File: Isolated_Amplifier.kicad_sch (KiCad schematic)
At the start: 12 parts, among them U3 AMC3311QDWERQ1

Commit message: isolated precharge from fuse
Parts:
- added C15: 1n, Capacitor_SMD:C_0603_1608Metric_Pad1.08x0.95mm_HandSolder, symbol Device:C
- renumbered C15 to C16, C16 to C17, C17 to C18, C18 to C19
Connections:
- net DCDC_OUT: now also C15.1
- net HVGND: now also C15.2
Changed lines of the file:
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@@
+	(wire
+		(pts
+			(xy 39.37 74.93) (xy 39.37 77.47)
+		)
+		(stroke
+			(width 0)
+			(type default)
+		)
+	)
 	(wire
 		(pts
@@
 	(wire
 		(pts
+			(xy 39.37 85.09) (xy 39.37 88.9)
+		)
+		(stroke
+			(width 0)
+			(type default)
+		)
+	)
+	(wire
+		(pts
 			(xy 137.16 45.72) (xy 137.16 50.8)
 		)
@@
 		)
 	)
-	(label "ISO_AMP"
+	(label "DCDC_HGND"
 		(at 16.51 25.4 0)
 		(effects
@@
 		)
 	)
-	(label "ISO_AMP"
+	(label "DCDC_HGND"
 		(at 16.51 45.72 0)
 		(effects
@@
 		)
 	)
+	(label "DCDC_OUT"
+		(at 39.37 74.93 180)
+		(effects
+			(font
+				(size 1.27 1.27)
+			)
+			(justify right bottom)
+		)
+	)
 	(label "HLDO_IN"
 		(at 46.99 35.56 180)
@@
 		)
 	)
-	(label "ISO_AMP"
+	(label "DCDC_HGND"
 		(at 52.07 31.75 0)
 		(effects
@@
 			)
 			(justify left)
+		)
+	)
+	(hierarchical_label "HVGND"
+		(shape bidirectional)
+		(at 39.37 88.9 180)
+		(effects
+			(font
+				(size 1.27 1.27)
+			)
+			(justify right)
 		)
 	)
@@
 			(project "PS-PrechargeBoard"
 				(path "/74d17fe6-68d4-4bd7-954a-e2bbb58b1f1e/6627985a-aef4-4302-9d05-a969136ea8f4/03979947-561d-482f-9fca-eedcd558d33d"
-					(reference "C20")
+					(reference "C21")
 					(unit 1)
 				)
@@
 				)
 				(path "/74d17fe6-68d4-4bd7-954a-e2bbb58b1f1e/c9d052f0-39c4-441f-8d4e-0430a3425be4/03979947-561d-482f-9fca-eedcd558d33d"
-					(reference "C65")
+					(reference "C68")
 					(unit 1)
 				)
 				(path "/74d17fe6-68d4-4bd7-954a-e2bbb58b1f1e/c9d052f0-39c4-441f-8d4e-0430a3425be4/4cf09e58-0892-4fb3-a566-fe1392b5d663"
-					(reference "C57")
+					(reference "C59")
 					(unit 1)
 				)
@@
 		(in_pos_files yes)
 		(dnp no)
-		(property "Reference" "C18"
+		(property "Reference" "C19"
 			(at 167.894 37.084 90)
 			(show_name no)
@@
 			(project "PS-PrechargeBoard"
 				(path "/74d17fe6-68d4-4bd7-954a-e2bbb58b1f1e/6627985a-aef4-4302-9d05-a969136ea8f4/03979947-561d-482f-9fca-eedcd558d33d"
-					(reference "C26")
+					(reference "C28")
 					(unit 1)
 				)
 				(path "/74d17fe6-68d4-4bd7-954a-e2bbb58b1f1e/6627985a-aef4-4302-9d05-a969136ea8f4/4cf09e58-0892-4fb3-a566-fe1392b5d663"
-					(reference "C18")
+					(reference "C19")
 					(unit 1)
 				)
 				(path "/74d17fe6-68d4-4bd7-954a-e2bbb58b1f1e/c9d052f0-39c4-441f-8d4e-0430a3425be4/03979947-561d-482f-9fca-eedcd558d33d"
-					(reference "C71")
+					(reference "C75")
 					(unit 1)
 				)
 				(path "/74d17fe6-68d4-4bd7-954a-e2bbb58b1f1e/c9d052f0-39c4-441f-8d4e-0430a3425be4/4cf09e58-0892-4fb3-a566-fe1392b5d663"
-					(reference "C63")
+					(reference "C66")
 					(unit 1)
 				)
@@
 			(project "PS-PrechargeBoard"
 				(path "/74d17fe6-68d4-4bd7-954a-e2bbb58b1f1e/6627985a-aef4-4302-9d05-a969136ea8f4/03979947-561d-482f-9fca-eedcd558d33d"
-					(reference "C19")
+					(reference "C20")
 					(unit 1)
 				)
@@
 				)
 				(path "/74d17fe6-68d4-4bd7-954a-e2bbb58b1f1e/c9d052f0-39c4-441f-8d4e-0430a3425be4/03979947-561d-482f-9fca-eedcd558d33d"
-					(reference "C64")
+					(reference "C67")
 					(unit 1)
 				)
 				(path "/74d17fe6-68d4-4bd7-954a-e2bbb58b1f1e/c9d052f0-39c4-441f-8d4e-0430a3425be4/4cf09e58-0892-4fb3-a566-fe1392b5d663"
-					(reference "C56")
+					(reference "C58")
 					(unit 1)
 				)
@@
 			(project "PS-PrechargeBoard"
 				(path "/74d17fe6-68d4-4bd7-954a-e2bbb58b1f1e/6627985a-aef4-4302-9d05-a969136ea8f4/03979947-561d-482f-9fca-eedcd558d33d"
-					(reference "C22")
+					(reference "C23")
 					(unit 1)
 				)
@@
 				)
 				(path "/74d17fe6-68d4-4bd7-954a-e2bbb58b1f1e/c9d052f0-39c4-441f-8d4e-0430a3425be4/03979947-561d-482f-9fca-eedcd558d33d"
-					(reference "C67")
+					(reference "C70")
 					(unit 1)
 				)
 				(path "/74d17fe6-68d4-4bd7-954a-e2bbb58b1f1e/c9d052f0-39c4-441f-8d4e-0430a3425be4/4cf09e58-0892-4fb3-a566-fe1392b5d663"
-					(reference "C59")
+					(reference "C61")
 					(unit 1)
 				)
@@
 		(in_pos_files yes)
 		(dnp no)
-		(property "Reference" "C15"
+		(property "Reference" "C16"
 			(at 142.24 21.844 90)
 			(show_name no)
@@
 			(project "PS-PrechargeBoard"
 				(path "/74d17fe6-68d4-4bd7-954a-e2bbb58b1f1e/6627985a-aef4-4302-9d05-a969136ea8f4/03979947-561d-482f-9fca-eedcd558d33d"
-					(reference "C23")
+					(reference "C25")
 					(unit 1)
 				)
 				(path "/74d17fe6-68d4-4bd7-954a-e2bbb58b1f1e/6627985a-aef4-4302-9d05-a969136ea8f4/4cf09e58-0892-4fb3-a566-fe1392b5d663"
-					(reference "C15")
+					(reference "C16")
 					(unit 1)
 				)
 				(path "/74d17fe6-68d4-4bd7-954a-e2bbb58b1f1e/c9d052f0-39c4-441f-8d4e-0430a3425be4/03979947-561d-482f-9fca-eedcd558d33d"
-					(reference "C68")
+					(reference "C72")
 					(unit 1)
 				)
 				(path "/74d17fe6-68d4-4bd7-954a-e2bbb58b1f1e/c9d052f0-39c4-441f-8d4e-0430a3425be4/4cf09e58-0892-4fb3-a566-fe1392b5d663"
-					(reference "C60")
+					(reference "C63")
 					(unit 1)
 				)
@@
 			(project "PS-PrechargeBoard"
 				(path "/74d17fe6-68d4-4bd7-954a-e2bbb58b1f1e/6627985a-aef4-4302-9d05-a969136ea8f4/03979947-561d-482f-9fca-eedcd558d33d"
-					(reference "C21")
+					(reference "C22")
 					(unit 1)
 				)
@@
 				)
 				(path "/74d17fe6-68d4-4bd7-954a-e2bbb58b1f1e/c9d052f0-39c4-441f-8d4e-0430a3425be4/03979947-561d-482f-9fca-eedcd558d33d"
-					(reference "C66")
+					(reference "C69")
 					(unit 1)
 				)
 				(path "/74d17fe6-68d4-4bd7-954a-e2bbb58b1f1e/c9d052f0-39c4-441f-8d4e-0430a3425be4/4cf09e58-0892-4fb3-a566-fe1392b5d663"
-					(reference "C58")
+					(reference "C60")
 					(unit 1)
 				)
@@
 		(in_pos_files yes)
 		(dnp no)
-		(property "Reference" "C17"
+		(property "Reference" "C18"
 			(at 142.24 42.164 90)
 			(show_name no)
@@
 			(project "PS-PrechargeBoard"
 				(path "/74d17fe6-68d4-4bd7-954a-e2bbb58b1f1e/6627985a-aef4-4302-9d05-a969136ea8f4/03979947-561d-482f-9fca-eedcd558d33d"
-					(reference "C25")
+					(reference "C27")
 					(unit 1)
 				)
 				(path "/74d17fe6-68d4-4bd7-954a-e2bbb58b1f1e/6627985a-aef4-4302-9d05-a969136ea8f4/4cf09e58-0892-4fb3-a566-fe1392b5d663"
-					(reference "C17")
+					(reference "C18")
 					(unit 1)
 				)
 				(path "/74d17fe6-68d4-4bd7-954a-e2bbb58b1f1e/c9d052f0-39c4-441f-8d4e-0430a3425be4/03979947-561d-482f-9fca-eedcd558d33d"
-					(reference "C70")
+					(reference "C74")
+					(unit 1)
+				)
+				(path "/74d17fe6-68d4-4bd7-954a-e2bbb58b1f1e/c9d052f0-39c4-441f-8d4e-0430a3425be4/4cf09e58-0892-4fb3-a566-fe1392b5d663"
+					(reference "C65")
+					(unit 1)
+				)
+			)
+		)
+	)
+	(symbol
+		(lib_id "Device:C")
+		(at 39.37 81.28 0)
+		(unit 1)
+		(body_style 1)
+		(exclude_from_sim no)
+		(in_bom yes)
+		(on_board yes)
+		(in_pos_files yes)
+		(dnp no)
+		(property "Reference" "C15"
+			(at 35.814 81.28 90)
+			(show_name no)
+			(do_not_autoplace no)
+			(effects
+				(font
+					(size 1.27 1.27)
+				)
+			)
+		)
+		(property "Value" "1n"
+			(at 42.926 81.28 90)
+			(show_name no)
+			(do_not_autoplace no)
+			(effects
+				(font
+					(size 1.27 1.27)
+				)
+			)
+		)
+		(property "Footprint" "Capacitor_SMD:C_0603_1608Metric_Pad1.08x0.95mm_HandSolder"
+			(at 40.3352 85.09 0)
+			(hide yes)
+			(show_name no)
+			(do_not_autoplace no)
+			(effects
+				(font
+					(size 1.27 1.27)
+				)
+			)
+		)
+		(property "Datasheet" ""
+			(at 39.37 81.28 0)
+			(hide yes)
+			(show_name no)
+			(do_not_autoplace no)
+			(effects
+				(font
+					(size 1.27 1.27)
+				)
+			)
+		)
+		(property "Description" "Unpolarized capacitor"
+			(at 39.37 81.28 0)
+			(hide yes)
+			(show_name no)
+			(do_not_autoplace no)
+			(effects
+				(font
+					(size 1.27 1.27)
+				)
+			)
+		)
+		(property "P/N" "MLASU063SB7102KFNA01"
+			(at 39.37 81.28 90)
+			(hide yes)
+			(show_name no)
+			(do_not_autoplace no)
+			(effects
+				(font
+					(size 1.27 1.27)
+				)
+			)
+		)
+		(pin "2"
+		)
+		(pin "1"
+		)
+		(instances
+			(project "PS-PrechargeBoard"
+				(path "/74d17fe6-68d4-4bd7-954a-e2bbb58b1f1e/6627985a-aef4-4302-9d05-a969136ea8f4/03979947-561d-482f-9fca-eedcd558d33d"
+					(reference "C24")
+					(unit 1)
+				)
+				(path "/74d17fe6-68d4-4bd7-954a-e2bbb58b1f1e/6627985a-aef4-4302-9d05-a969136ea8f4/4cf09e58-0892-4fb3-a566-fe1392b5d663"
+					(reference "C15")
+					(unit 1)
+				)
+				(path "/74d17fe6-68d4-4bd7-954a-e2bbb58b1f1e/c9d052f0-39c4-441f-8d4e-0430a3425be4/03979947-561d-482f-9fca-eedcd558d33d"
+					(reference "C71")
 					(unit 1)
 				)
@@
 		(in_pos_files yes)
 		(dnp no)
-		(property "Reference" "C16"
+		(property "Reference" "C17"
 			(at 142.24 32.004 90)
 			(show_name no)
@@
 			(project "PS-PrechargeBoard"
 				(path "/74d17fe6-68d4-4bd7-954a-e2bbb58b1f1e/6627985a-aef4-4302-9d05-a969136ea8f4/03979947-561d-482f-9fca-eedcd558d33d"
-					(reference "C24")
+					(reference "C26")
 					(unit 1)
 				)
 				(path "/74d17fe6-68d4-4bd7-954a-e2bbb58b1f1e/6627985a-aef4-4302-9d05-a969136ea8f4/4cf09e58-0892-4fb3-a566-fe1392b5d663"
-					(reference "C16")
+					(reference "C17")
 					(unit 1)
 				)
 				(path "/74d17fe6-68d4-4bd7-954a-e2bbb58b1f1e/c9d052f0-39c4-441f-8d4e-0430a3425be4/03979947-561d-482f-9fca-eedcd558d33d"
-					(reference "C69")
+					(reference "C73")
 					(unit 1)
 				)
 				(path "/74d17fe6-68d4-4bd7-954a-e2bbb58b1f1e/c9d052f0-39c4-441f-8d4e-0430a3425be4/4cf09e58-0892-4fb3-a566-fe1392b5d663"
-					(reference "C61")
-					(unit 1)
-				)
+					(reference "C64")
+					(unit 1)
+				)

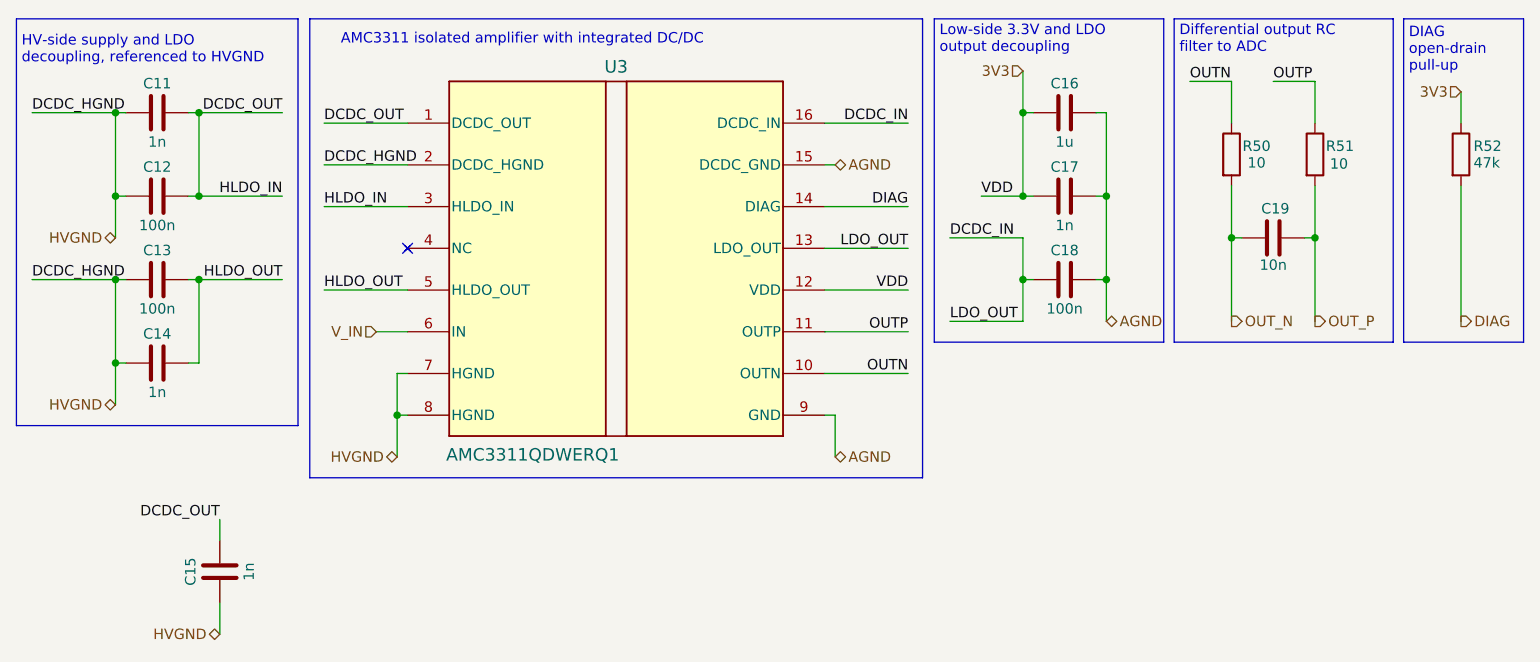
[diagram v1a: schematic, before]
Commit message: voltage sensor cleanup
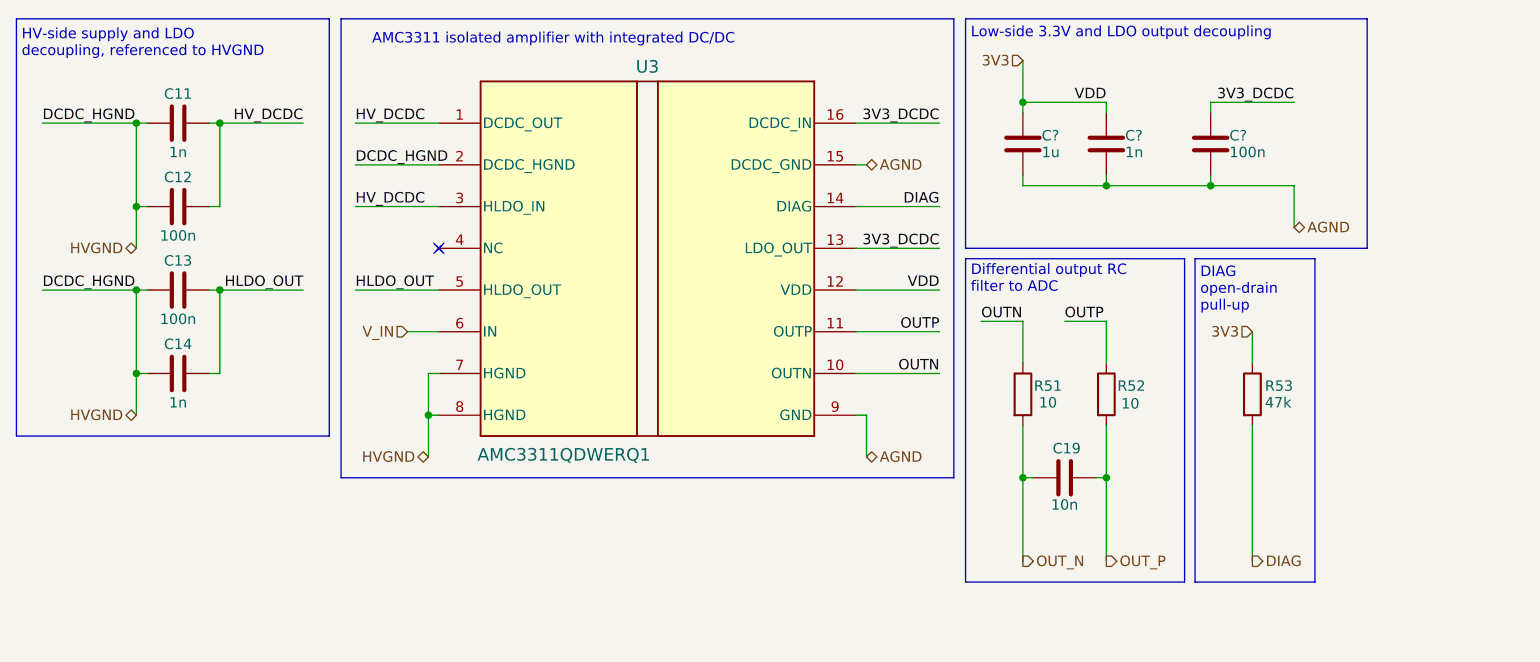
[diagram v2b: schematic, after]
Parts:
- removed C15, C17: 1n, Capacitor_SMD:C_0603_1608Metric_Pad1.08x0.95mm_HandSolder, symbol Device:C
- removed C16: 1u, Capacitor_SMD:C_0603_1608Metric_Pad1.08x0.95mm_HandSolder, symbol Device:C
- removed C18: 100n, Capacitor_SMD:C_0603_1608Metric_Pad1.08x0.95mm_HandSolder, symbol Device:C
- added C?: 100n, Capacitor_SMD:C_0603_1608Metric_Pad1.08x0.95mm_HandSolder, symbol Device:C
- added C?: 1n, Capacitor_SMD:C_0603_1608Metric_Pad1.08x0.95mm_HandSolder, symbol Device:C
- added C?: 1u, Capacitor_SMD:C_0603_1608Metric_Pad1.08x0.95mm_HandSolder, symbol Device:C
- renumbered R50 to R51, R51 to R52, R52 to R53
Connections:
- net 3V3: now also C?.1, C?.1
- net AGND: now also C?.1, C?.2, C?.2
- net DCDC_IN renamed 3V3_DCDC
- net 3V3_DCDC: now also C?.2
- net DCDC_OUT renamed HV_DCDC
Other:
- moved on the sheet: C11, C12, C13, C14, C19, R51, R52, R53, U3

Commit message: updated usb-c connector
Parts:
- gave numbers to parts that had none: 3
- renumbered C19 to C11, C11 to C6, C12 to C7, C13 to C8, C14 to C9, R51 to R27, R52 to R28, R53 to R29, U3 to U2

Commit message: footprints & schematic cute-ification
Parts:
- U2: footprint AMC3311QDWERQ1:DWE0016A-IPC_A -> Precharge:SOIC127P1030X265-16N
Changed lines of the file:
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@@
 			)
 		)
-		(property "Footprint" "AMC3311QDWERQ1:DWE0016A-IPC_A"
+		(property "Footprint" "Precharge:SOIC127P1030X265-16N"
 			(at 66.04 26.67 0)
 			(hide yes)

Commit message: finished schematic & footprint
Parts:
- U2: value AMC3311QDWERQ1 -> (none); footprint Precharge:SOIC127P1030X265-16N -> Precharge_Board:SOIC127P1030X265-16N
- renumbered R27 to R26, R28 to R27, R29 to R28
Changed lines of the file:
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@@
 		(in_pos_files yes)
 		(dnp no)
-		(property "Reference" "R28"
+		(property "Reference" "R27"
 			(at 150.368 58.674 0)
 			(show_name no)
@@
 			(project "PS-PrechargeBoard"
 				(path "/74d17fe6-68d4-4bd7-954a-e2bbb58b1f1e/6627985a-aef4-4302-9d05-a969136ea8f4/03979947-561d-482f-9fca-eedcd558d33d"
-					(reference "R31")
+					(reference "R30")
 					(unit 1)
 				)
 				(path "/74d17fe6-68d4-4bd7-954a-e2bbb58b1f1e/6627985a-aef4-4302-9d05-a969136ea8f4/4cf09e58-0892-4fb3-a566-fe1392b5d663"
-					(reference "R28")
+					(reference "R27")
 					(unit 1)
 				)
 				(path "/74d17fe6-68d4-4bd7-954a-e2bbb58b1f1e/c9d052f0-39c4-441f-8d4e-0430a3425be4/03979947-561d-482f-9fca-eedcd558d33d"
-					(reference "R61")
+					(reference "R60")
 					(unit 1)
 				)
 				(path "/74d17fe6-68d4-4bd7-954a-e2bbb58b1f1e/c9d052f0-39c4-441f-8d4e-0430a3425be4/4cf09e58-0892-4fb3-a566-fe1392b5d663"
-					(reference "R58")
+					(reference "R57")
 					(unit 1)
 				)
@@
 		(in_pos_files yes)
 		(dnp no)
-		(property "Reference" "R27"
+		(property "Reference" "R26"
 			(at 140.208 58.674 0)
 			(show_name no)
@@
 			(project "PS-PrechargeBoard"
 				(path "/74d17fe6-68d4-4bd7-954a-e2bbb58b1f1e/6627985a-aef4-4302-9d05-a969136ea8f4/03979947-561d-482f-9fca-eedcd558d33d"
-					(reference "R30")
+					(reference "R29")
 					(unit 1)
 				)
 				(path "/74d17fe6-68d4-4bd7-954a-e2bbb58b1f1e/6627985a-aef4-4302-9d05-a969136ea8f4/4cf09e58-0892-4fb3-a566-fe1392b5d663"
-					(reference "R27")
+					(reference "R26")
 					(unit 1)
 				)
 				(path "/74d17fe6-68d4-4bd7-954a-e2bbb58b1f1e/c9d052f0-39c4-441f-8d4e-0430a3425be4/03979947-561d-482f-9fca-eedcd558d33d"
-					(reference "R60")
+					(reference "R59")
 					(unit 1)
 				)
 				(path "/74d17fe6-68d4-4bd7-954a-e2bbb58b1f1e/c9d052f0-39c4-441f-8d4e-0430a3425be4/4cf09e58-0892-4fb3-a566-fe1392b5d663"
-					(reference "R57")
+					(reference "R56")
 					(unit 1)
 				)
@@
 		(in_pos_files yes)
 		(dnp no)
-		(property "Reference" "R29"
+		(property "Reference" "R28"
 			(at 166.624 58.674 0)
 			(show_name no)
@@
 			(project "PS-PrechargeBoard"
 				(path "/74d17fe6-68d4-4bd7-954a-e2bbb58b1f1e/6627985a-aef4-4302-9d05-a969136ea8f4/03979947-561d-482f-9fca-eedcd558d33d"
-					(reference "R32")
+					(reference "R31")
 					(unit 1)
 				)
 				(path "/74d17fe6-68d4-4bd7-954a-e2bbb58b1f1e/6627985a-aef4-4302-9d05-a969136ea8f4/4cf09e58-0892-4fb3-a566-fe1392b5d663"
-					(reference "R29")
+					(reference "R28")
 					(unit 1)
 				)
 				(path "/74d17fe6-68d4-4bd7-954a-e2bbb58b1f1e/c9d052f0-39c4-441f-8d4e-0430a3425be4/03979947-561d-482f-9fca-eedcd558d33d"
-					(reference "R62")
+					(reference "R61")
 					(unit 1)
 				)
 				(path "/74d17fe6-68d4-4bd7-954a-e2bbb58b1f1e/c9d052f0-39c4-441f-8d4e-0430a3425be4/4cf09e58-0892-4fb3-a566-fe1392b5d663"
-					(reference "R59")
+					(reference "R58")
 					(unit 1)
 				)
@@
 			)
 		)
-		(property "Value" "AMC3311QDWERQ1"
+		(property "Value" ""
 			(at 81.28 67.056 0)
 			(show_name no)
@@
 			)
 		)
-		(property "Footprint" "Precharge:SOIC127P1030X265-16N"
+		(property "Footprint" "Precharge_Board:SOIC127P1030X265-16N"
 			(at 66.04 26.67 0)
 			(hide yes)

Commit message: fixed hv placement
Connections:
- net AGND renamed GND
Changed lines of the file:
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@@
 		)
 	)
-	(hierarchical_label "AGND"
+	(hierarchical_label "GND"
 		(shape bidirectional)
 		(at 170.18 39.37 0)
@@
 		)
 	)
-	(hierarchical_label "AGND"
+	(hierarchical_label "GND"
 		(shape bidirectional)
 		(at 118.11 67.31 0)
@@
 		)
 	)
-	(hierarchical_label "AGND"
+	(hierarchical_label "GND"
 		(shape bidirectional)
 		(at 118.11 31.75 0)
